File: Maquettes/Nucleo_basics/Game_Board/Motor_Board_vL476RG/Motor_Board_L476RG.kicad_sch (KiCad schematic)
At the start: 43 parts, among them CON1 MikroE-nRF-S-module, J1 LCD_SD, J10 3.3V_reg, J2 JoyStick, J3 AnalogIn, J4 BAT_IN, J5 Morpho_Gauche, J6 Morpho_Droite, J7 I2C_Visu, J8 I2C_EXT, J9 GND_reg, SW1 SW_1, SW2 SW_2, SW3 SW_3, SW4 SW_4, SW5 SW_5, U1 MCP23008-xP

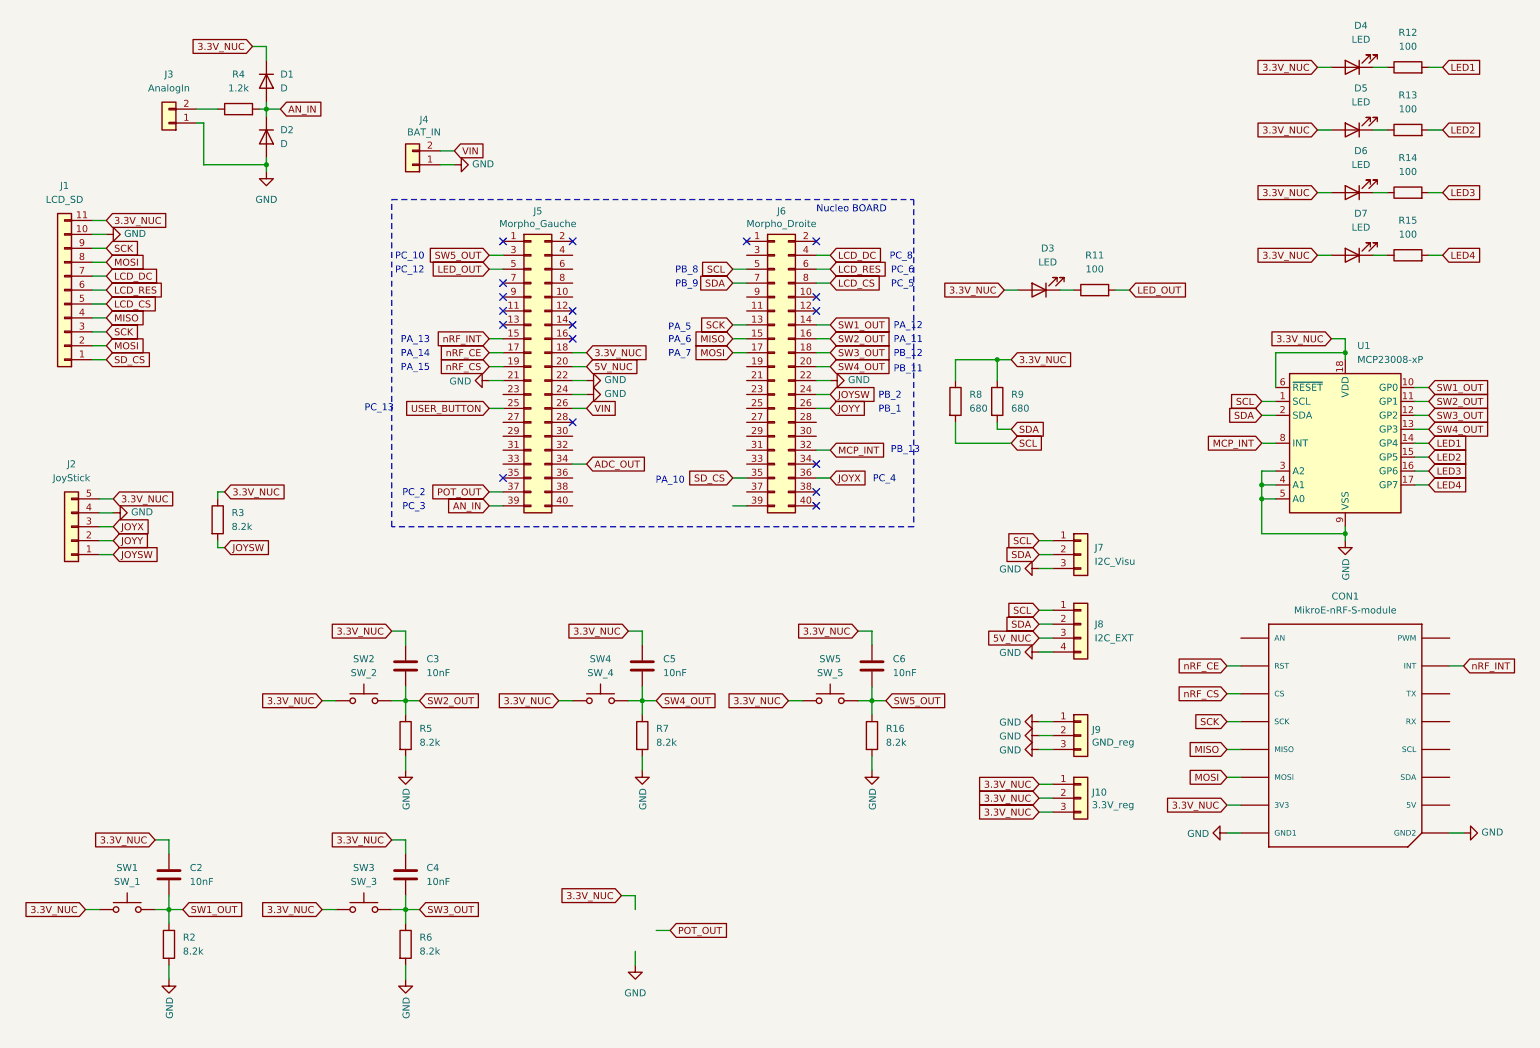
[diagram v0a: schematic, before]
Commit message: Update Remote and Robot Nucleo basics
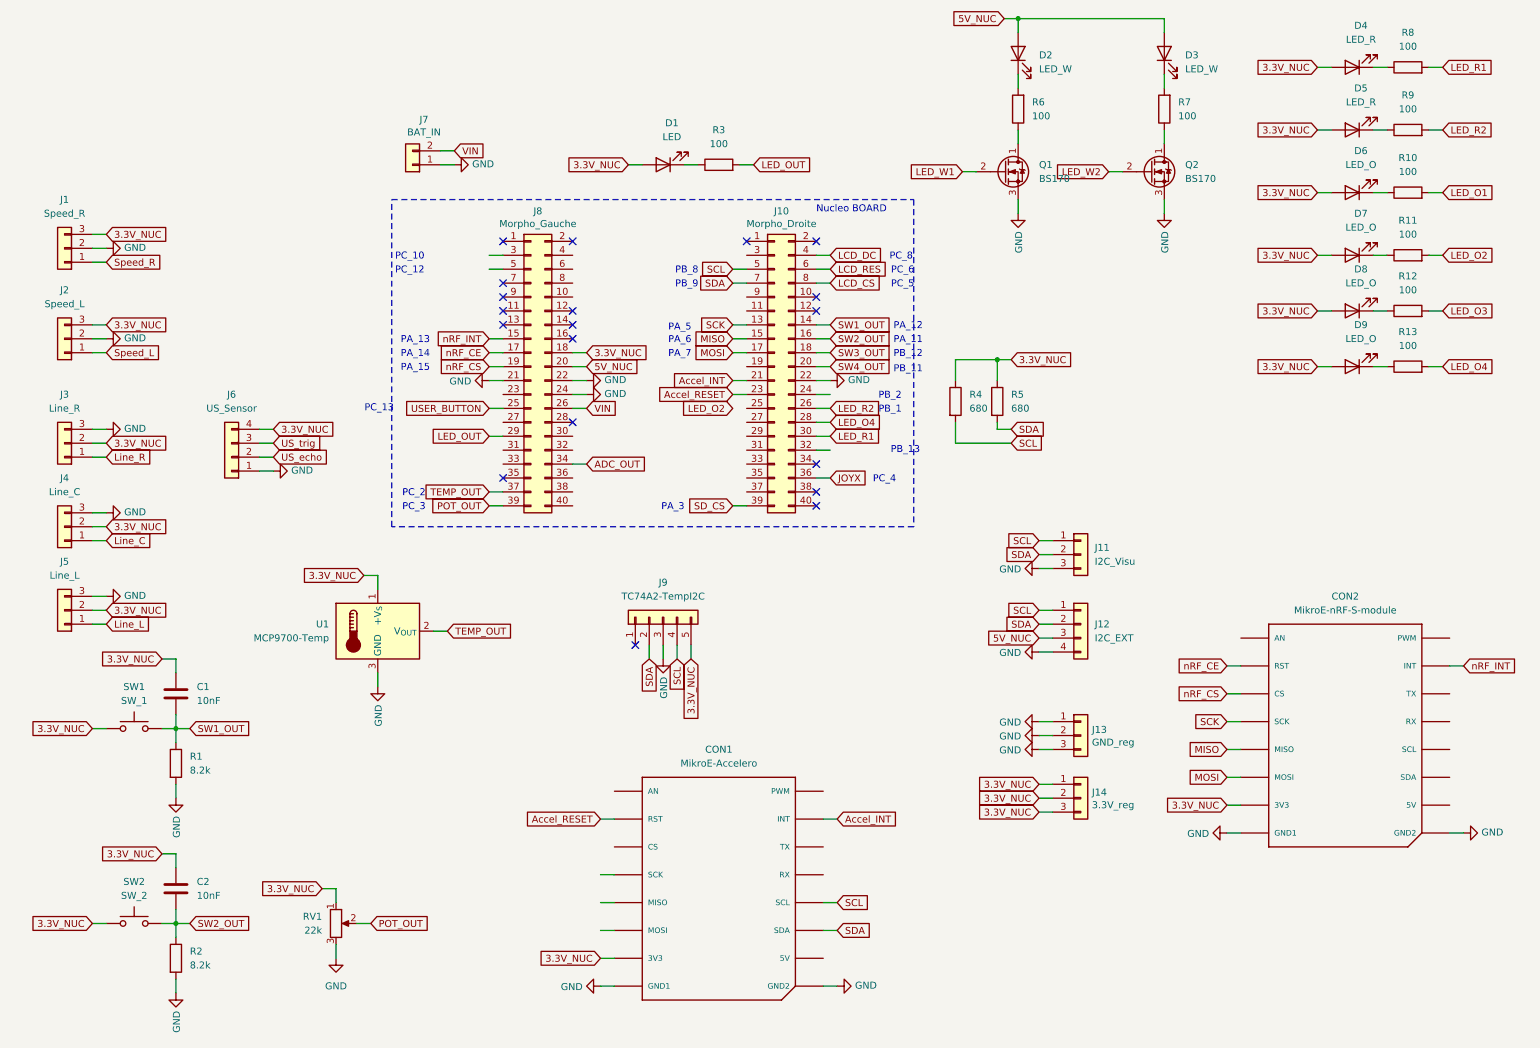
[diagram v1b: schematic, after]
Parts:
- removed C3, C4, C5, C6: 10nF, Capacitor_THT:C_Rect_L7.0mm_W3.5mm_P5.00mm, symbol Device:C
- removed D1, D2: D, Diode_THT:D_DO-35_SOD27_P7.62mm_Horizontal, symbol Device:D
- removed J1: LCD_SD, Connector_PinSocket_2.54mm:PinSocket_1x11_P2.54mm_Horizontal, symbol Connector_Generic:Conn_01x11
- removed J2: JoyStick, Connector_PinSocket_2.54mm:PinSocket_1x05_P2.54mm_Horizontal, symbol Connector_Generic:Conn_01x05
- removed J3: AnalogIn, Connector_PinSocket_2.54mm:PinSocket_1x02_P2.54mm_Horizontal, symbol Connector_Generic:Conn_01x02
- removed R16, R3, R5: 8.2k, Resistor_THT:R_Axial_DIN0207_L6.3mm_D2.5mm_P10.16mm_Horizontal, symbol Device:R
- removed R4: 1.2k, Resistor_THT:R_Axial_DIN0207_L6.3mm_D2.5mm_P10.16mm_Horizontal, symbol Device:R
- removed SW3: SW_3, LEnsE_devices:Switch, symbol Switch:SW_Push
- removed SW4: SW_4, LEnsE_devices:Switch, symbol Switch:SW_Push
- removed SW5: SW_5, LEnsE_devices:Switch, symbol Switch:SW_Push
- removed U1: MCP23008-xP, Package_DIP:DIP-18_W7.62mm, symbol Interface_Expansion:MCP23008-xP
- added C2: 10nF, Capacitor_THT:C_Rect_L7.0mm_W3.5mm_P5.00mm, symbol Device:C
- added CON1: MikroE-Accelero, mikroE:MIKROBUS_MODULE_CONN, symbol mikroBUS:MIKROBUS_MODULE_CONN
- added D2, D3: LED_W, LED_THT:LED_D3.0mm_Clear, symbol Device:LED
- added D8, D9: LED_O, LED_THT:LED_D3.0mm_Clear, symbol Device:LED
- added J1: Speed_R, Connector_PinSocket_2.54mm:PinSocket_1x03_P2.54mm_Horizontal, symbol Connector_Generic:Conn_01x03
- added J2: Speed_L, Connector_PinSocket_2.54mm:PinSocket_1x03_P2.54mm_Horizontal, symbol Connector_Generic:Conn_01x03
- added J3: Line_R, Connector_PinSocket_2.54mm:PinSocket_1x03_P2.54mm_Horizontal, symbol Connector_Generic:Conn_01x03
- added J4: Line_C, Connector_PinSocket_2.54mm:PinSocket_1x03_P2.54mm_Horizontal, symbol Connector_Generic:Conn_01x03
- added J5: Line_L, Connector_PinSocket_2.54mm:PinSocket_1x03_P2.54mm_Horizontal, symbol Connector_Generic:Conn_01x03
- added J6: US_Sensor, Connector_PinSocket_2.54mm:PinSocket_1x04_P2.54mm_Vertical, symbol Connector_Generic:Conn_01x04
- added J9: TC74A2-TempI2C, Package_TO_SOT_THT:TO-220-5_Vertical, symbol Connector_Generic:Conn_01x05
- added Q1, Q2: BS170, Package_TO_SOT_THT:TO-92_Inline, symbol Transistor_FET:BS170
- added R12, R13: 100, Resistor_THT:R_Axial_DIN0207_L6.3mm_D2.5mm_P10.16mm_Horizontal, symbol Device:R
- added R2: 8.2k, Resistor_THT:R_Axial_DIN0207_L6.3mm_D2.5mm_P10.16mm_Horizontal, symbol Device:R
- added RV1: 22k, Potentiometer_THT:Potentiometer_Bourns_3386P_Vertical, symbol Device:R_Potentiometer
- added U1: MCP9700-Temp, Package_TO_SOT_THT:TO-92_Inline, symbol Sensor_Temperature:LM35-LP
- CON2: renamed from CON1; footprint miKro:MIKROBUS_MODULE_CONN -> mikroE:MIKROBUS_MODULE_CONN
- D4, D5: value LED -> LED_R
- D6, D7: value LED -> LED_O
- R6, R7: value 8.2k -> 100
- SW1, SW2: footprint LEnsE_devices:Switch -> LEnsE:Switch
- renumbered C2 to C1, D3 to D1, J6 to J10, J7 to J11, J8 to J12, J9 to J13, J10 to J14, J4 to J7, J5 to J8, R2 to R1, R14 to R10, R15 to R11, R11 to R3, R8 to R4, R9 to R5, R12 to R8, R13 to R9
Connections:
- net AN_IN is gone; now on net POT_OUT: J8.39 (Pin_39)
- net LED1 is gone; now on net LED_R1: R8.2
- net LED2 is gone; now on net LED_R2: R9.2
- net 3.3V_NUC: now also C2.1, CON1.P7 (3V3), D8.2 (A), D9.2 (A), J1.3 (Pin_3), J2.3 (Pin_3), J3.2 (Pin_2), J4.2 (Pin_2), J5.2 (Pin_2), J6.4 (Pin_4), J9.5 (Pin_5), RV1.1, U1.1 (+V_{S})
- net 5V_NUC: now also D2.2 (A), D3.2 (A)
- net GND: now also CON1.P8 (GND1), CON1.P9 (GND2), J1.2 (Pin_2), J2.2 (Pin_2), J3.3 (Pin_3), J4.3 (Pin_3), J5.3 (Pin_3), J6.1 (Pin_1), J9.3 (Pin_3), Q1.3 (S), Q2.3 (S), R2.2, RV1.3, U1.3 (GND); no longer R6.2, R7.2
- net LED_OUT: now also J8.29 (Pin_29); no longer J8.5 (Pin_5)
- net POT_OUT: now also RV1.2; no longer J8.37 (Pin_37)
- net SCL: now also CON1.P12 (SCL), J9.4 (Pin_4)
- net SDA: now also CON1.P11 (SDA), J9.2 (Pin_2)
- net SD_CS: now also J10.39 (Pin_39); no longer J10.35 (Pin_35)
- net SW2_OUT: now also C2.2, R2.1
- net SW3_OUT: no longer R6.1
- net SW4_OUT: no longer R7.1
- net Accel_INT: now reaches J10.21 (Pin_21)
- net Accel_INT: now also CON1.P15 (INT)
- net Accel_RESET: now reaches J10.23 (Pin_23)
- net Accel_RESET: now also CON1.P2 (RST)
- net LED_O4: now reaches J10.28 (Pin_28)
- net LED_O4: now also R13.2
- net LED_R1: now reaches J10.30 (Pin_30)
- net JOYSW: no longer names the net of J10.24 (Pin_24)
- net JOYY renamed LED_R2
- net LED3 renamed LED_O1
- net LED4 renamed LED_O2
- net MCP_INT: no longer names the net of J10.32 (Pin_32)
- net SW5_OUT: no longer names the net of J8.3 (Pin_3)
- new net: Q2.1 (D), R7.1
- new net: D9.1 (K), R13.1
- new net: D3.1 (K), R7.2
- new net: Q1.1 (D), R6.1
- new net: D2.1 (K), R6.2
- new net: D8.1 (K), R12.1
- new net LED_O3: R12.2
- new net LED_W1: Q1.2 (G)
- new net LED_W2: Q2.2 (G)
- new net Line_C: J4.1 (Pin_1)
- new net Line_L: J5.1 (Pin_1)
- new net Line_R: J3.1 (Pin_1)
- new net Speed_L: J2.1 (Pin_1)
- new net Speed_R: J1.1 (Pin_1)
- new net TEMP_OUT: J8.37 (Pin_37), U1.2 (V_{OUT})
- new net US_echo: J6.2 (Pin_2)
- new net US_trig: J6.3 (Pin_3)
- no-connect marks 18 -> 19
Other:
- note added: "PA_3"
- note removed: "PA_10"
- moved on the sheet: C1, D1, R1, R3, SW1

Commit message: Update Robot Board
ATTENTION : Déplacer la carte Nucléo (ou changer sens mais bcp de modif...)
Tester SPI avec MISO:PC_11, MISO:PC_12, SCK:PC_10
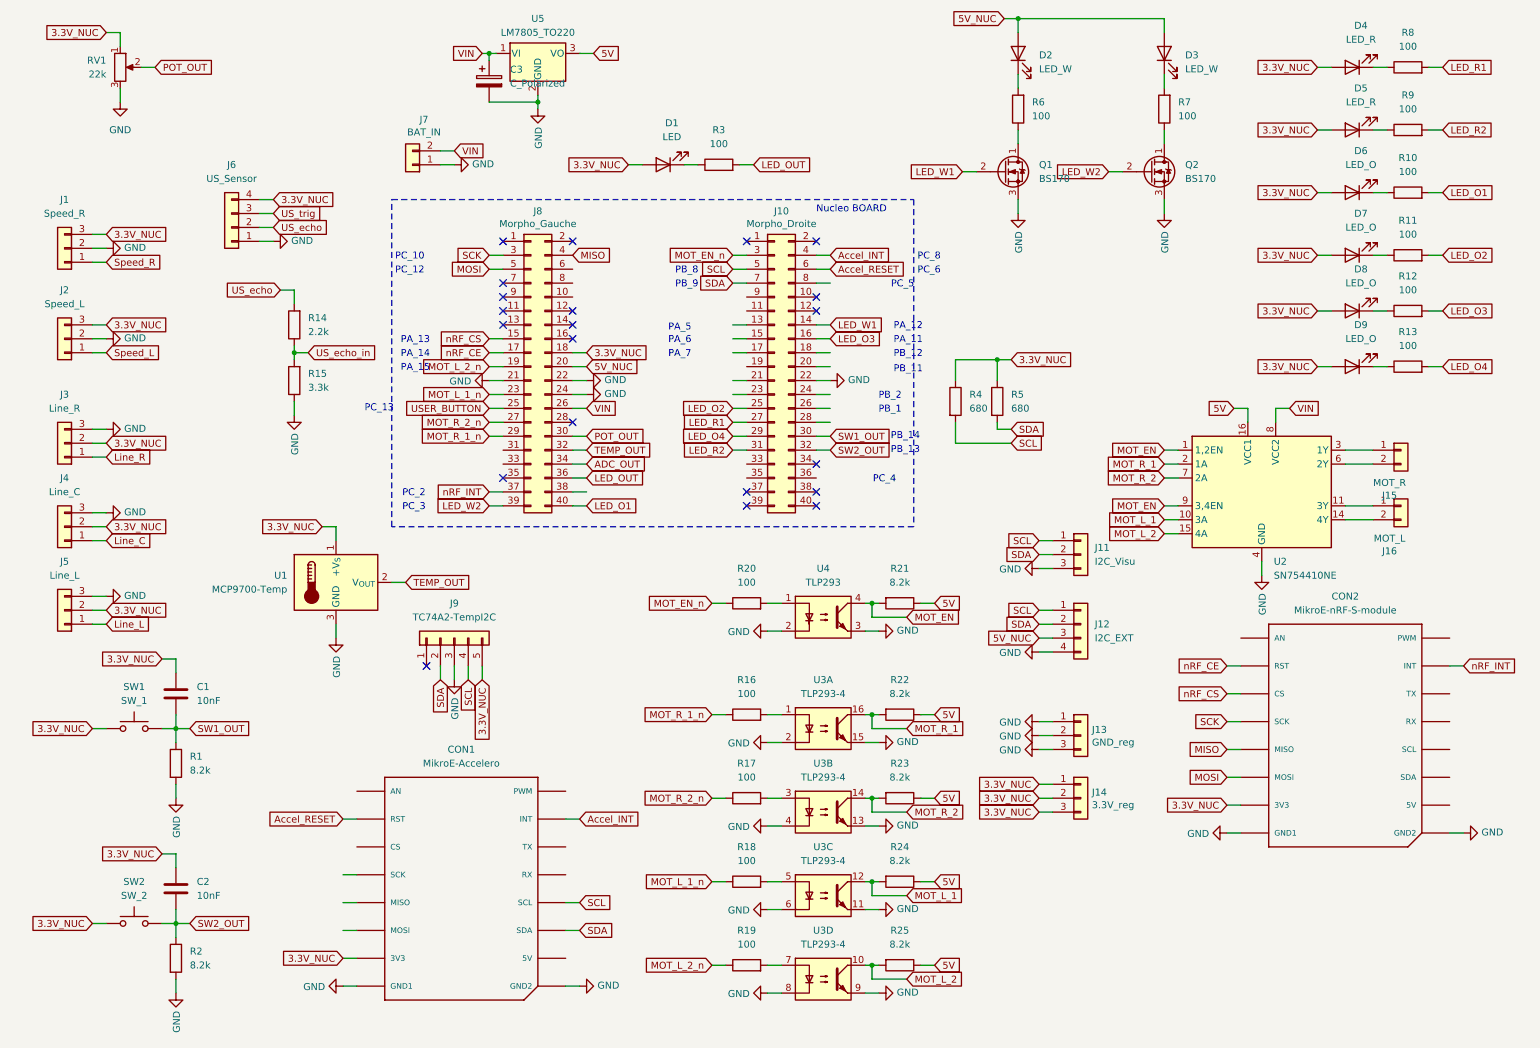
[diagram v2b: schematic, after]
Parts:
- added C3: C_Polarized, Capacitor_THT:CP_Radial_D6.3mm_P2.50mm, symbol Device:C_Polarized
- added J15: MOT_R, TerminalBlock_Phoenix:TerminalBlock_Phoenix_MKDS-3-2-5.08_1x02_P5.08mm_Horizontal, symbol Connector_Generic:Conn_01x02
- added J16: MOT_L, TerminalBlock_Phoenix:TerminalBlock_Phoenix_MKDS-3-2-5.08_1x02_P5.08mm_Horizontal, symbol Connector_Generic:Conn_01x02
- added R14: 2.2k, Resistor_THT:R_Axial_DIN0207_L6.3mm_D2.5mm_P10.16mm_Horizontal, symbol Device:R
- added R15: 3.3k, Resistor_THT:R_Axial_DIN0207_L6.3mm_D2.5mm_P10.16mm_Horizontal, symbol Device:R
- added R16, R17, R18, R19, R20: 100, Resistor_THT:R_Axial_DIN0207_L6.3mm_D2.5mm_P10.16mm_Horizontal, symbol Device:R
- added R21, R22, R23, R24, R25: 8.2k, Resistor_THT:R_Axial_DIN0207_L6.3mm_D2.5mm_P10.16mm_Horizontal, symbol Device:R
- added U2: SN754410NE, Package_DIP:DIP-16_W7.62mm, symbol Driver_Motor:SN754410NE
- added U3: TLP293-4, Package_SO:SOIC-16_4.55x10.3mm_P1.27mm, symbol Isolator:TLP293-4
- added U4: TLP293, Package_SO:SOIC-4_4.55x2.6mm_P1.27mm, symbol Isolator:TLP293
- added U5: LM7805_TO220, Package_TO_SOT_THT:TO-220-3_Vertical, symbol Regulator_Linear:LM7805_TO220
- CON1, CON2: footprint mikroE:MIKROBUS_MODULE_CONN -> miKroE:MIKROBUS_MODULE_CONN
- J12: footprint Connector_PinSocket_2.54mm:PinSocket_1x04_P2.54mm_Horizontal -> Connector_PinSocket_2.54mm:PinSocket_1x04_P2.54mm_Vertical
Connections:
- net LCD_DC is gone; now on net Accel_INT: J10.4 (Pin_4)
- net LCD_RES is gone; now on net Accel_RESET: J10.6 (Pin_6)
- net Accel_INT: no longer J10.21 (Pin_21)
- net Accel_RESET: no longer J10.23 (Pin_23)
- net GND: now also C3.2, R15.1, U2.12 (GND), U2.13 (GND), U2.4 (GND), U2.5 (GND), U3.11, U3.13, U3.15, U3.2, U3.4, U3.6, U3.8, U3.9, U4.2, U4.3, U5.2 (GND)
- net LED_O1: now also J8.40 (Pin_40)
- net LED_O2: now also J10.25 (Pin_25)
- net LED_O3: now also J10.16 (Pin_16)
- net LED_O4: now also J10.29 (Pin_29); no longer J10.28 (Pin_28)
- net LED_OUT: now also J8.36 (Pin_36); no longer J8.29 (Pin_29)
- net LED_R1: now also J10.27 (Pin_27); no longer J10.30 (Pin_30)
- net LED_R2: now also J10.31 (Pin_31); no longer J10.26 (Pin_26)
- net LED_W1: now also J10.14 (Pin_14)
- net LED_W2: now also J8.39 (Pin_39)
- net MISO: now also J8.4 (Pin_4); no longer J10.15 (Pin_15)
- net MOSI: now also J8.5 (Pin_5); no longer J10.17 (Pin_17)
- net POT_OUT: now also J8.30 (Pin_30); no longer J8.39 (Pin_39)
- net SCK: now also J8.3 (Pin_3); no longer J10.13 (Pin_13)
- net SW1_OUT: now also J10.30 (Pin_30); no longer J10.14 (Pin_14)
- net SW2_OUT: now also J10.32 (Pin_32); no longer J10.16 (Pin_16)
- net TEMP_OUT: now also J8.32 (Pin_32); no longer J8.37 (Pin_37)
- net US_echo: now also R14.2
- net VIN: now also C3.1, U2.8 (VCC2), U5.1 (VI)
- net nRF_CS: now also J8.15 (Pin_15); no longer J8.19 (Pin_19)
- net nRF_INT: now also J8.37 (Pin_37); no longer J8.15 (Pin_15)
- net MOT_L_1_n: now reaches J8.23 (Pin_23)
- net MOT_L_1_n: now also R18.1
- net MOT_R_2_n: now reaches J8.27 (Pin_27)
- net MOT_R_2_n: now also R17.1
- net MOT_EN_n: now reaches J10.3 (Pin_3)
- net MOT_EN_n: now also R20.1
- net JOYX: no longer names the net of J10.36 (Pin_36)
- net LCD_CS: no longer names the net of J10.8 (Pin_8)
- net SD_CS: no longer names the net of J10.39 (Pin_39)
- net SW3_OUT: no longer names the net of J10.18 (Pin_18)
- net SW4_OUT: no longer names the net of J10.20 (Pin_20)
- new net: R16.2, U3.1
- new net: J16.1 (Pin_1), U2.11 (3Y)
- new net: J16.2 (Pin_2), U2.14 (4Y)
- new net: J15.1 (Pin_1), U2.3 (1Y)
- new net: J15.2 (Pin_2), U2.6 (2Y)
- new net: R20.2, U4.1
- new net: R17.2, U3.3
- new net: R19.2, U3.7
- new net: R18.2, U3.5
- new net 5V: R21.1, R22.1, R23.1, R24.1, R25.1, U2.16 (VCC1), U5.3 (VO)
- new net MOT_EN: R21.2, U2.1 (1,2EN), U2.9 (3,4EN), U4.4
- new net MOT_L_1: R24.2, U2.10 (3A), U3.12
- new net MOT_L_2: R25.2, U2.15 (4A), U3.10
- new net MOT_L_2_n: J8.19 (Pin_19), R19.1
- new net MOT_R_1: R22.2, U2.2 (1A), U3.16
- new net MOT_R_1_n: J8.29 (Pin_29), R16.1
- new net MOT_R_2: R23.2, U2.7 (2A), U3.14
- new net US_echo_in: R14.1, R15.2
- no-connect marks 19 -> 21
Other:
- note added: "PB_14"
- note removed: "PA_3"
- moved on the sheet: CON1, J6, J9, RV1, U1
